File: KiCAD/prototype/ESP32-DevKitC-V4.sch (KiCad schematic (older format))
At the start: 14 parts

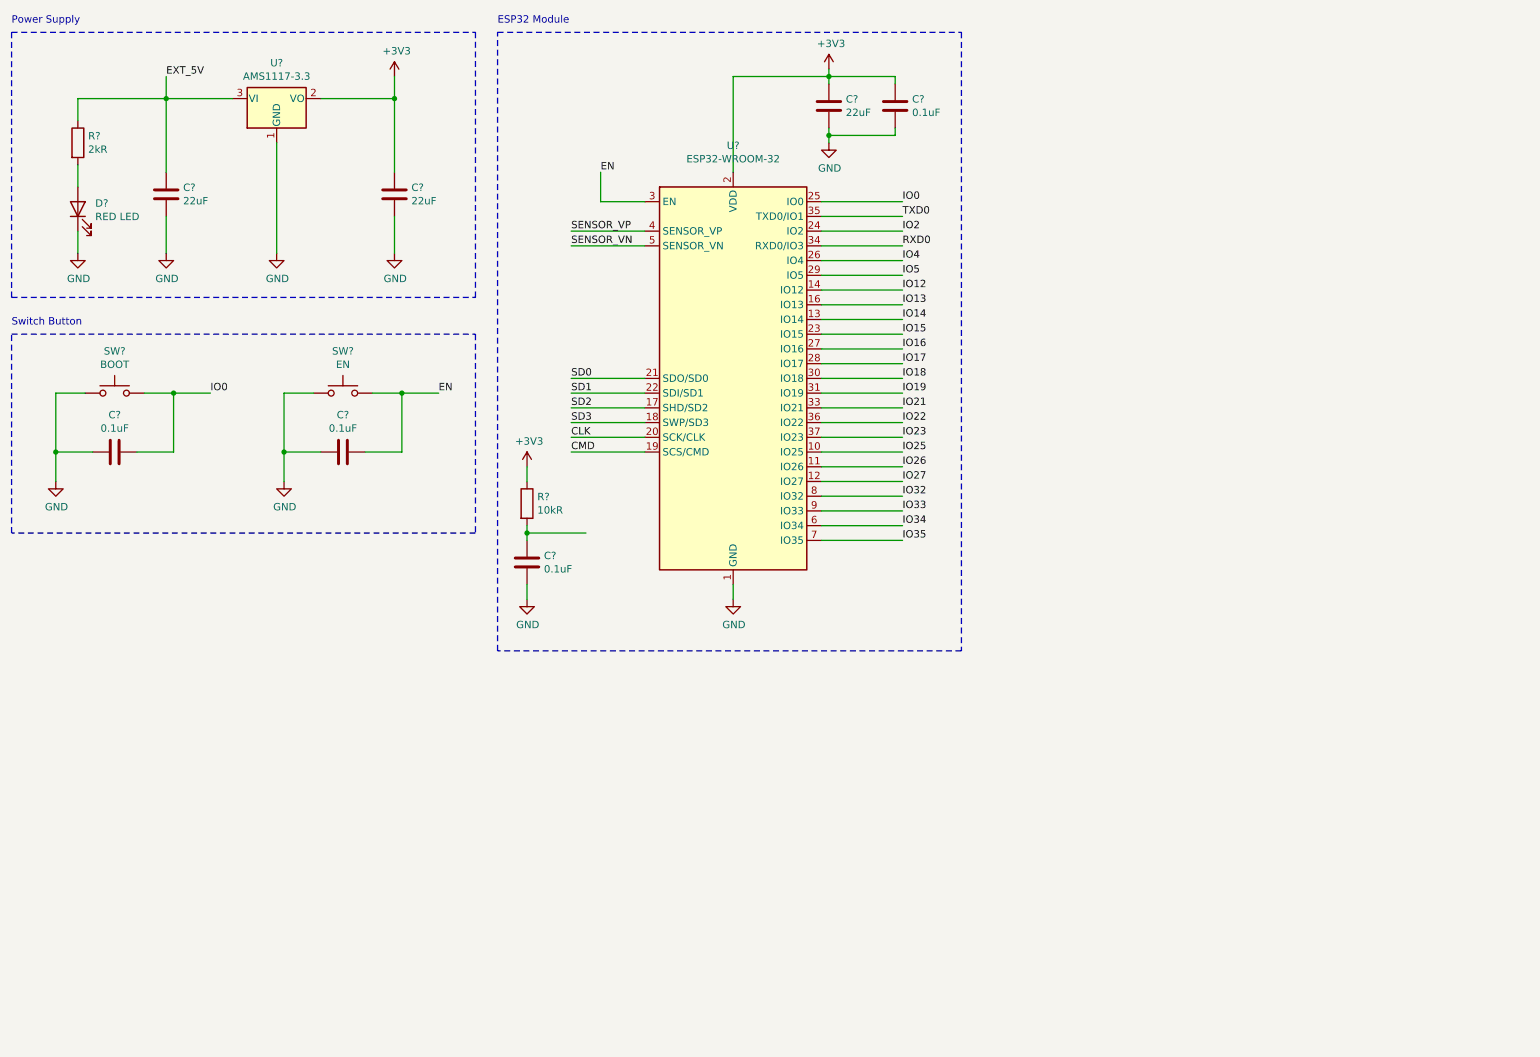
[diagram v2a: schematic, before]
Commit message: Add connector connections
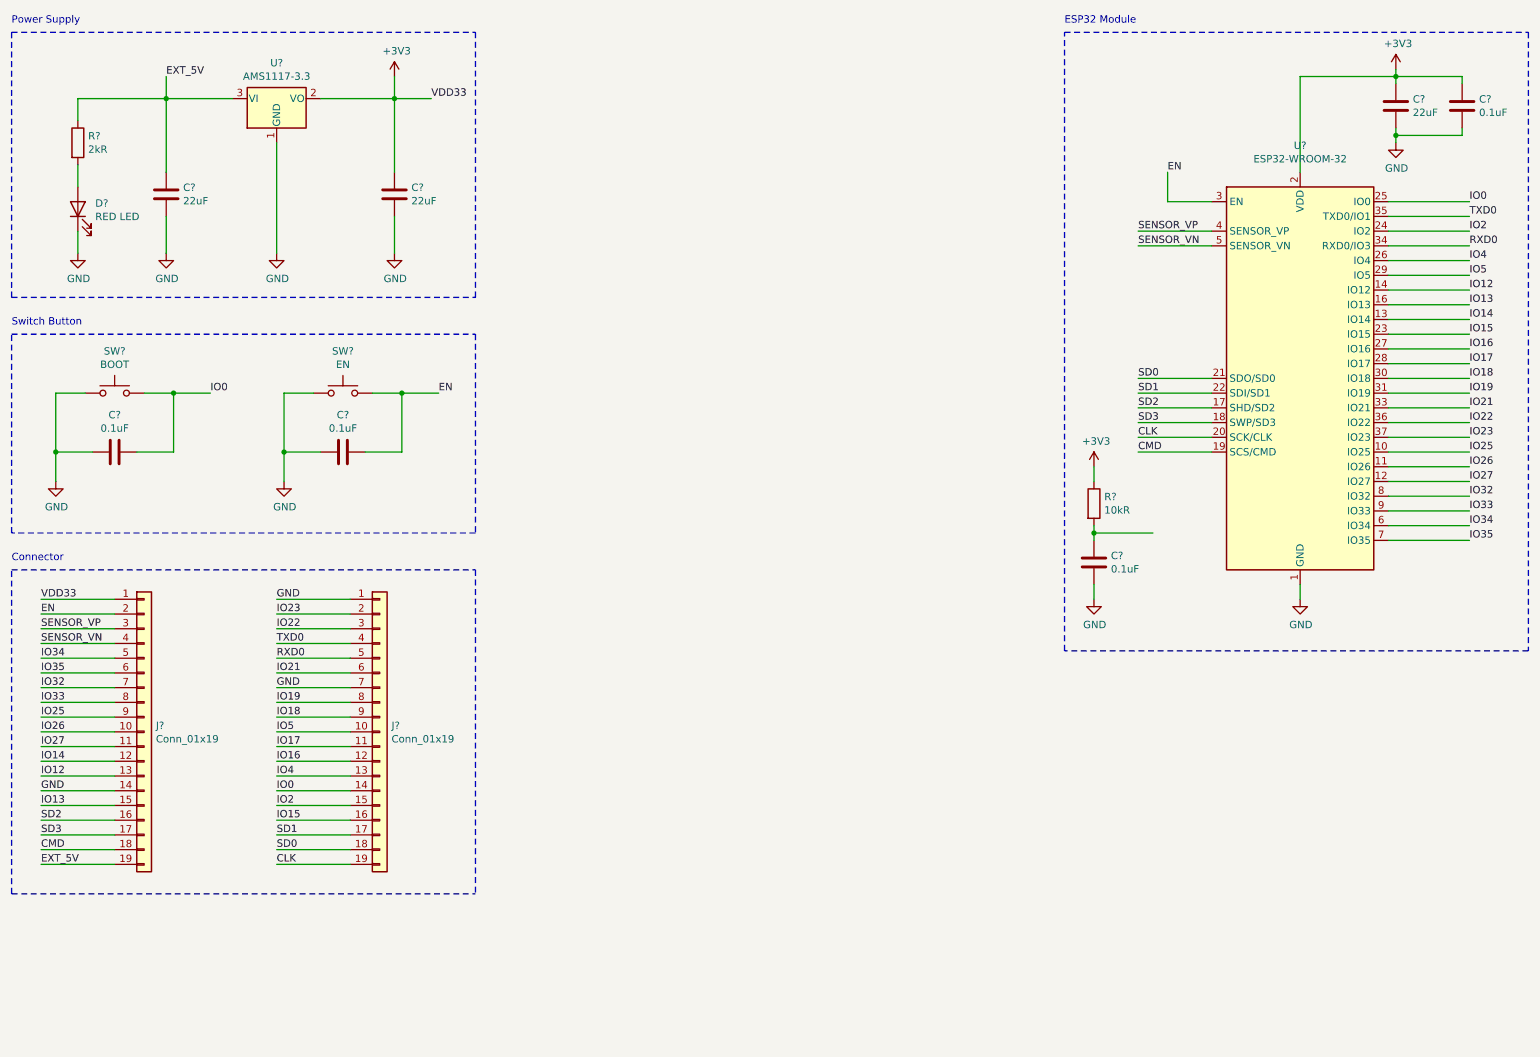
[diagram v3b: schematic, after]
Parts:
- added J? (x2): Conn_01x19, symbol Connector_Generic:Conn_01x19
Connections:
- net +3V3: now also J?.1 (Pin_1)
- net CLK: now also J?.19 (Pin_19)
- net CMD: now also J?.18 (Pin_18)
- net EN: now also J?.2 (Pin_2)
- net EXT_5V: now also J?.19 (Pin_19)
- net GND: now also J?.1 (Pin_1), J?.14 (Pin_14), J?.7 (Pin_7)
- net IO0: now also J?.14 (Pin_14)
- net IO12: now also J?.13 (Pin_13)
- net IO13: now also J?.15 (Pin_15)
- net IO14: now also J?.12 (Pin_12)
- net IO15: now also J?.16 (Pin_16)
- net IO16: now also J?.12 (Pin_12)
- net IO17: now also J?.11 (Pin_11)
- net IO18: now also J?.9 (Pin_9)
- net IO19: now also J?.8 (Pin_8)
- net IO2: now also J?.15 (Pin_15)
- net IO21: now also J?.6 (Pin_6)
- net IO22: now also J?.3 (Pin_3)
- net IO23: now also J?.2 (Pin_2)
- net IO25: now also J?.9 (Pin_9)
- net IO26: now also J?.10 (Pin_10)
- net IO27: now also J?.11 (Pin_11)
- net IO32: now also J?.7 (Pin_7)
- net IO33: now also J?.8 (Pin_8)
- net IO34: now also J?.5 (Pin_5)
- net IO35: now also J?.6 (Pin_6)
- net IO4: now also J?.13 (Pin_13)
- net IO5: now also J?.10 (Pin_10)
- net RXD0: now also J?.5 (Pin_5)
- net SD0: now also J?.18 (Pin_18)
- net SD1: now also J?.17 (Pin_17)
- net SD2: now also J?.16 (Pin_16)
- net SD3: now also J?.17 (Pin_17)
- net SENSOR_VN: now also J?.4 (Pin_4)
- net SENSOR_VP: now also J?.3 (Pin_3)
- net TXD0: now also J?.4 (Pin_4)
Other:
- note added: "Connector"
- moved on the sheet: C?, R?, U?

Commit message: Add initial USB connections and circuits
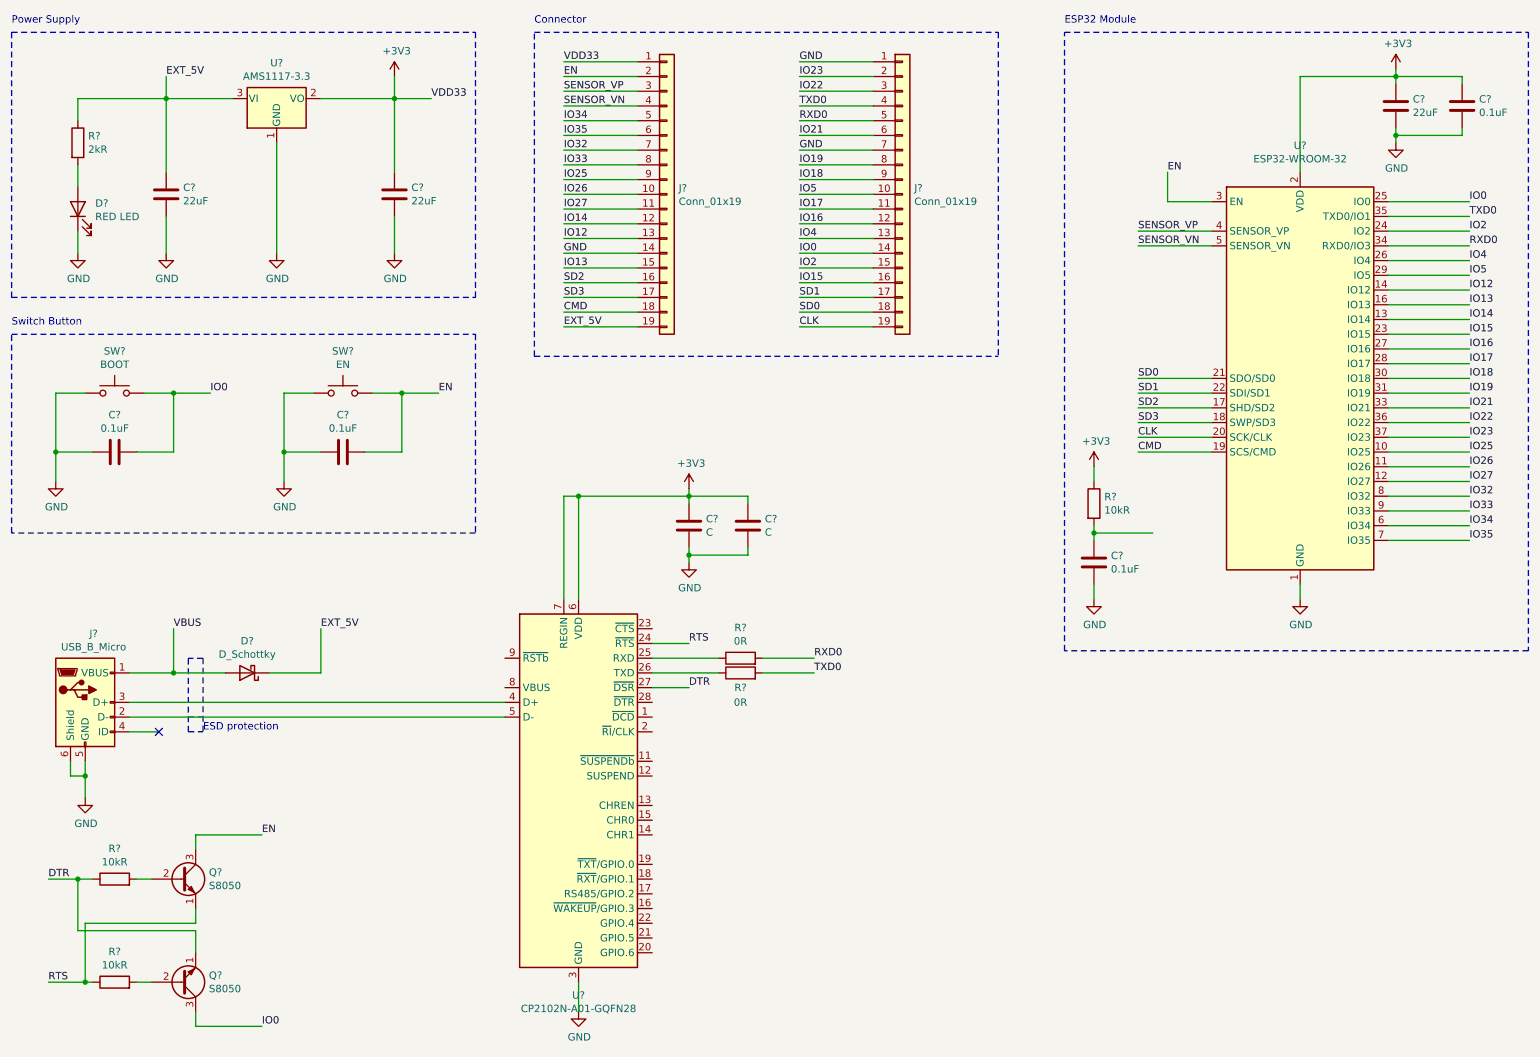
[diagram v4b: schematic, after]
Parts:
- added C? (x2): C, symbol Device:C
- added D?: D_Schottky, symbol Device:D_Schottky
- added J?: USB_B_Micro, symbol Connector:USB_B_Micro
- added Q? (x2): S8050, Package_TO_SOT_THT:TO-92_Inline, symbol Transistor_BJT:S8050
- added R? (x2): 0R, symbol Device:R
- added R? (x2): 10kR, symbol Device:R
- added U?: CP2102N-A01-GQFN28, Package_DFN_QFN:QFN-28-1EP_5x5mm_P0.5mm_EP3.35x3.35mm, symbol Interface_USB:CP2102N-A01-GQFN28
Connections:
- net +3V3: now also C?.1, C?.1, U?.6 (VDD), U?.7 (REGIN)
- net EN: now also Q?.3 (C)
- net EXT_5V: now also D?.1 (K)
- net GND: now also C?.2, C?.2, J?.5 (GND), J?.6 (Shield), U?.29 (GND), U?.3 (GND)
- net IO0: now also Q?.3 (C)
- net RXD0: now also R?.2
- net TXD0: now also R?.2
- new net: R?.1, U?.25 (RXD)
- new net: R?.1, U?.26 (TXD)
- new net: J?.3 (D+), U?.4 (D+)
- new net: J?.2 (D-), U?.5 (D-)
- new net: Q?.2 (B), R?.2 (x2)
- new net DTR: Q?.1 (E), R?.1, U?.27 (~DSR)
- new net RTS: Q?.1 (E), R?.1, U?.24 (~RTS)
- new net VBUS: D?.2 (A), J?.1 (VBUS)
- no-connect marks 0 -> 1
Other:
- note added: "ESD protection"
- moved on the sheet: J?

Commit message: Change local labels to hierarchical labels
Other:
- moved on the sheet: C?, R?
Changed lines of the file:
@@
 L power:+3V3 #PWR?
 U 1 1 5F9419AA
-P 8050 3650
-F 0 "#PWR?" H 8050 3500 50  0001 C CNN
-F 1 "+3V3" H 8065 3823 50  0000 C CNN
-F 2 "" H 8050 3650 50  0001 C CNN
-F 3 "" H 8050 3650 50  0001 C CNN
-	1    8050 3650
+P 8200 3900
+F 0 "#PWR?" H 8200 3750 50  0001 C CNN
+F 1 "+3V3" H 8215 4073 50  0000 C CNN
+F 2 "" H 8200 3900 50  0001 C CNN
+F 3 "" H 8200 3900 50  0001 C CNN
+	1    8200 3900
 	1    0    0    -1
 $EndComp
@@
 L Device:R R?
 U 1 1 5F94208F
-P 8050 3900
-F 0 "R?" H 8120 3946 50  0000 L CNN
-F 1 "10kR" H 8120 3855 50  0000 L CNN
-F 2 "" V 7980 3900 50  0001 C CNN
-F 3 "~" H 8050 3900 50  0001 C CNN
-	1    8050 3900
+P 8200 4150
+F 0 "R?" H 8270 4196 50  0000 L CNN
+F 1 "10kR" H 8270 4105 50  0000 L CNN
+F 2 "" V 8130 4150 50  0001 C CNN
+F 3 "~" H 8200 4150 50  0001 C CNN
+	1    8200 4150
 	1    0    0    -1
 $EndComp
@@
 L Device:C C?
 U 1 1 5F9429EB
-P 8050 4300
-F 0 "C?" H 8165 4346 50  0000 L CNN
-F 1 "0.1uF" H 8165 4255 50  0000 L CNN
-F 2 "" H 8088 4150 50  0001 C CNN
-F 3 "~" H 8050 4300 50  0001 C CNN
-F 4 "50V" H 8165 4255 50  0001 L CNN "Voltage"
-F 5 "10%" H 8165 4164 50  0001 L CNN "Tolerance"
-	1    8050 4300
+P 8200 4550
+F 0 "C?" H 8315 4596 50  0000 L CNN
+F 1 "0.1uF" H 8315 4505 50  0000 L CNN
+F 2 "" H 8238 4400 50  0001 C CNN
+F 3 "~" H 8200 4550 50  0001 C CNN
+F 4 "50V" H 8315 4505 50  0001 L CNN "Voltage"
+F 5 "10%" H 8315 4414 50  0001 L CNN "Tolerance"
+	1    8200 4550
 	1    0    0    -1
 $EndComp
@@
 L power:GND #PWR?
 U 1 1 5F942C61
-P 8050 4550
-F 0 "#PWR?" H 8050 4300 50  0001 C CNN
-F 1 "GND" H 8055 4377 50  0000 C CNN
-F 2 "" H 8050 4550 50  0001 C CNN
-F 3 "" H 8050 4550 50  0001 C CNN
-	1    8050 4550
-	1    0    0    -1
-$EndComp
-Wire Wire Line
-	8050 4550 8050 4450
-Wire Wire Line
-	8050 3750 8050 3650
+P 8200 4800
+F 0 "#PWR?" H 8200 4550 50  0001 C CNN
+F 1 "GND" H 8205 4627 50  0000 C CNN
+F 2 "" H 8200 4800 50  0001 C CNN
+F 3 "" H 8200 4800 50  0001 C CNN
+	1    8200 4800
+	1    0    0    -1
+$EndComp
+Wire Wire Line
+	8200 4800 8200 4700
+Wire Wire Line
+	8200 4000 8200 3900
 $Comp
 L power:+3V3 #PWR?
@@
 Wire Wire Line
 	10050 2150 10600 2150
-Text Label 10600 1950 0    50   ~ 0
-TXD0
-Text Label 10600 2150 0    50   ~ 0
-RXD0
 Wire Notes Line
 	7850 700  11000 700
 Wire Notes Line
-	11000 700  11000 4900
-Wire Notes Line
-	11000 4900 7850 4900
-Wire Notes Line
-	7850 4900 7850 700
+	11000 5100 7850 5100
 Text Notes 7850 650  0    50   ~ 0
 ESP32 Module
@@
 Wire Wire Line
 	10050 1850 10600 1850
-Text Label 10600 1850 0    50   ~ 0
-IO0
 Wire Wire Line
 	1800 3150 2050 3150
@@
 Connection ~ 3350 3150
 Wire Wire Line
-	8050 4050 8050 4100
-Connection ~ 8050 4100
-Wire Wire Line
-	8050 4100 8050 4150
-Wire Wire Line
-	8050 4100 8450 4100
-Wire Wire Line
-	8550 1650 8550 1850
-Wire Wire Line
-	8550 1850 8850 1850
-Text Label 8550 1650 0    50   ~ 0
-EN
+	8200 4300 8200 4350
+Connection ~ 8200 4350
+Wire Wire Line
+	8200 4350 8200 4400
+Wire Wire Line
+	8200 4350 8600 4350
 Wire Notes Line
 	700  2750 3850 2750
@@
 Wire Wire Line
 	10050 4150 10600 4150
-Wire Wire Line
-	8850 3050 8350 3050
-Wire Wire Line
-	8850 3150 8350 3150
-Wire Wire Line
-	8850 3250 8350 3250
-Wire Wire Line
-	8850 3350 8350 3350
-Wire Wire Line
-	8850 3450 8350 3450
-Wire Wire Line
-	8850 3550 8350 3550
-Text Label 8350 3050 0    50   ~ 0
-SD0
-Text Label 8350 3150 0    50   ~ 0
-SD1
-Text Label 8350 3250 0    50   ~ 0
-SD2
-Text Label 8350 3350 0    50   ~ 0
-SD3
-Text Label 8350 3450 0    50   ~ 0
-CLK
-Text Label 8350 3550 0    50   ~ 0
-CMD
-Wire Wire Line
-	8850 2150 8350 2150
-Wire Wire Line
-	8850 2050 8350 2050
-Text Label 8350 2050 0    50   ~ 0
-SENSOR_VP
-Text Label 8350 2150 0    50   ~ 0
-SENSOR_VN
-Text Label 10600 2050 0    50   ~ 0
-IO2
-Text Label 10600 2250 0    50   ~ 0
-IO4
-Text Label 10600 2350 0    50   ~ 0
-IO5
-Text Label 10600 2450 0    50   ~ 0
-IO12
-Text Label 10600 2550 0    50   ~ 0
-IO13
-Text Label 10600 2650 0    50   ~ 0
-IO14
-Text Label 10600 2750 0    50   ~ 0
-IO15
-Text Label 10600 2850 0    50   ~ 0
-IO16
-Text Label 10600 2950 0    50   ~ 0
-IO17
-Text Label 10600 3050 0    50   ~ 0
-IO18
-Text Label 10600 3150 0    50   ~ 0
-IO19
-Text Label 10600 3250 0    50   ~ 0
-IO21
-Text Label 10600 3350 0    50   ~ 0
-IO22
-Text Label 10600 3450 0    50   ~ 0
-IO23
-Text Label 10600 3550 0    50   ~ 0
-IO25
-Text Label 10600 3650 0    50   ~ 0
-IO26
-Text Label 10600 3750 0    50   ~ 0
-IO27
-Text Label 10600 3850 0    50   ~ 0
-IO32
-Text Label 10600 3950 0    50   ~ 0
-IO33
-Text Label 10600 4050 0    50   ~ 0
-IO34
-Text Label 10600 4150 0    50   ~ 0
-IO35
 $Comp
 L Connector_Generic:Conn_01x19 J?
@@
 Wire Wire Line
 	4950 2700 4450 2700
-Wire Wire Line
-	3300 1150 3550 1150
-Text Label 3550 1150 0    50   ~ 0
-VDD33
 Text Label 4450 900  0    50   ~ 0
 VDD33
@@
 	4450 3850 4550 3850
 Connection ~ 4550 3850
+Text HLabel 10600 1850 2    50   Input ~ 0
+IO0
+Text HLabel 10600 1950 2    50   Input ~ 0
+TXD0
+Text HLabel 10600 2050 2    50   Input ~ 0
+IO2
+Text HLabel 10600 2150 2    50   Input ~ 0
+RXD0
+Text HLabel 10600 2250 2    50   Input ~ 0
+IO4
+Text HLabel 10600 2350 2    50   Input ~ 0
+IO5
+Text HLabel 10600 2450 2    50   Input ~ 0
+IO12
+Text HLabel 10600 2550 2    50   Input ~ 0
+IO13
+Text HLabel 10600 2650 2    50   Input ~ 0
+IO14
+Text HLabel 10600 2750 2    50   Input ~ 0
+IO15
+Text HLabel 10600 2850 2    50   Input ~ 0
+IO16
+Text HLabel 10600 2950 2    50   Input ~ 0
+IO17
+Text HLabel 10600 3050 2    50   Input ~ 0
+IO18
+Text HLabel 10600 3150 2    50   Input ~ 0
+IO19
+Text HLabel 10600 3250 2    50   Input ~ 0
+IO21
+Text HLabel 10600 3350 2    50   Input ~ 0
+IO22
+Text HLabel 10600 3450 2    50   Input ~ 0
+IO23
+Text HLabel 10600 3550 2    50   Input ~ 0
+IO25
+Text HLabel 10600 3650 2    50   Input ~ 0
+IO26
+Text HLabel 10600 3750 2    50   Input ~ 0
+IO27
+Text HLabel 10600 3850 2    50   Input ~ 0
+IO32
+Text HLabel 10600 3950 2    50   Input ~ 0
+IO33
+Text HLabel 10600 4050 2    50   Input ~ 0
+IO34
+Text HLabel 10600 4150 2    50   Input ~ 0
+IO35
+Text HLabel 8450 2050 0    50   Input ~ 0
+SENSOR_VP
+Text HLabel 8450 2150 0    50   Input ~ 0
+SENSOR_VN
+Text HLabel 8450 3050 0    50   Input ~ 0
+SD0
+Text HLabel 8450 3150 0    50   Input ~ 0
+SD1
+Text HLabel 8450 3250 0    50   Input ~ 0
+SD2
+Text HLabel 8450 3350 0    50   Input ~ 0
+SD3
+Text HLabel 8450 3450 0    50   Input ~ 0
+CLK
+Text HLabel 8450 3550 0    50   Input ~ 0
+CMD
+Wire Notes Line
+	11000 700  11000 5100
+Wire Notes Line
+	7850 700  7850 5100
+Wire Wire Line
+	8850 2050 8450 2050
+Wire Wire Line
+	8450 2150 8850 2150
+Wire Wire Line
+	8850 3050 8450 3050
+Wire Wire Line
+	8850 3150 8450 3150
+Wire Wire Line
+	8850 3250 8450 3250
+Wire Wire Line
+	8850 3350 8450 3350
+Wire Wire Line
+	8850 3450 8450 3450
+Wire Wire Line
+	8850 3550 8450 3550
+Text HLabel 8450 1850 0    50   Input ~ 0
+EN
+Wire Wire Line
+	8450 1850 8850 1850
+Text HLabel 3500 1150 2    50   Input ~ 0
+VDD33
+Wire Wire Line
+	3500 1150 3300 1150
 $EndSCHEMATC

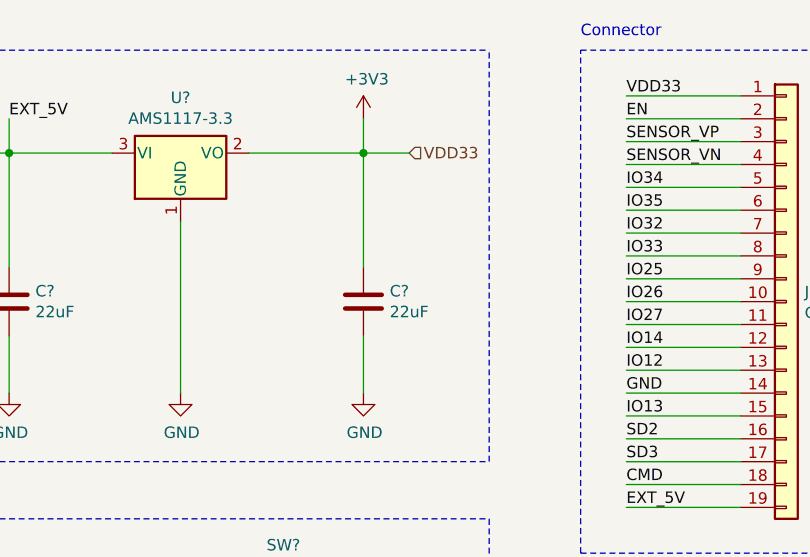
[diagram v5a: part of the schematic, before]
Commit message: Export all signals to the schematic reference
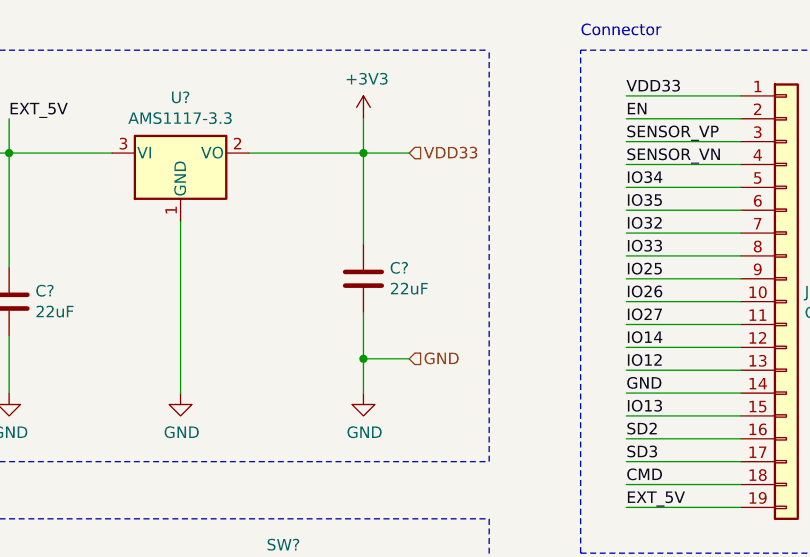
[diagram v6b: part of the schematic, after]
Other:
- moved on the sheet: C?
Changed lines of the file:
@@
 L Device:C C?
 U 1 1 5F9310B4
-P 3300 1800
-F 0 "C?" H 3415 1846 50  0000 L CNN
-F 1 "22uF" H 3415 1755 50  0000 L CNN
-F 2 "" H 3338 1650 50  0001 C CNN
-F 3 "~" H 3300 1800 50  0001 C CNN
-	1    3300 1800
-	1    0    0    -1
-$EndComp
-Wire Wire Line
-	3300 1650 3300 1150
+P 3300 1700
+F 0 "C?" H 3415 1746 50  0000 L CNN
+F 1 "22uF" H 3415 1655 50  0000 L CNN
+F 2 "" H 3338 1550 50  0001 C CNN
+F 3 "~" H 3300 1700 50  0001 C CNN
+	1    3300 1700
+	1    0    0    -1
+$EndComp
 Connection ~ 3300 1150
 $Comp
@@
 	1    0    0    -1
 $EndComp
-Wire Wire Line
-	3300 2200 3300 1950
 Wire Notes Line
 	3850 2500 3850 700
@@
 Wire Wire Line
 	3500 1150 3300 1150
+Wire Wire Line
+	3300 1550 3300 1150
+Wire Wire Line
+	3300 1850 3300 2050
+Wire Wire Line
+	3300 2050 3500 2050
+Connection ~ 3300 2050
+Wire Wire Line
+	3300 2050 3300 2200
+Text HLabel 3500 2050 2    50   Input ~ 0
+GND
 $EndSCHEMATC
